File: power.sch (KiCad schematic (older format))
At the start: 75 parts, among them J6 7-17 V IN, Q1 DMP3099L-7, SW7 JS202011SCQN, U1 ICE40HX4K-TQ144, U10 MAX40200AUK, U12 TPS562201, U15 MAX40200AUK, U21 MAX40200AUK, U6 TLV62568APDRLR, U7 TLV62568APDRLR

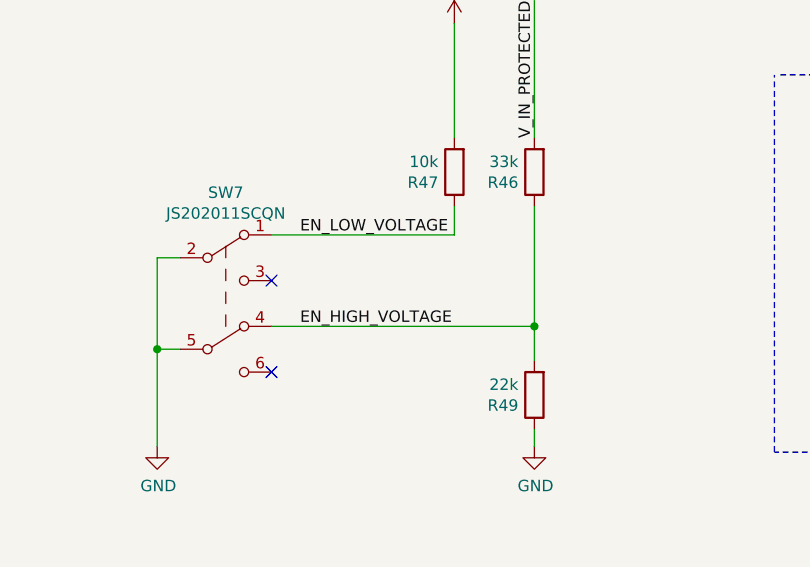
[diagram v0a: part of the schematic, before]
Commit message: Corrected a few footprints
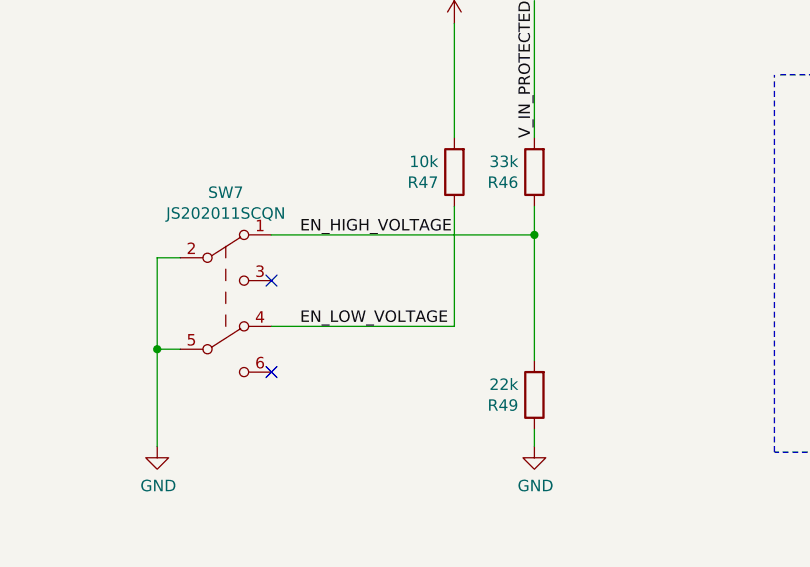
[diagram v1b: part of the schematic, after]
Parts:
- L3: footprint footprints:DLW5BTM_5.00x5.00mm_footprint -> footprints:L_Murata_DLW5BTM_5.00x5.00mm_footprint
- U6, U7: footprint Package_TO_SOT_SMD:SOT-563 -> footprints:Texas_DRL_SOT-563_1.6x1.6mm_0.5mm-pitch_footprint
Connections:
- net EN_HIGH_VOLTAGE: now also SW7.1 (A); no longer SW7.4 (A)
- net EN_LOW_VOLTAGE: now also SW7.4 (A); no longer SW7.1 (A)
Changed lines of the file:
@@
 F 0 "U6" H 2775 7815 50  0000 C CNN
 F 1 "TLV62568APDRLR" H 2775 7724 50  0000 C CNN
-F 2 "Package_TO_SOT_SMD:SOT-563" H 2775 7050 50  0001 C CNN
+F 2 "footprints:Texas_DRL_SOT-563_1.6x1.6mm_0.5mm-pitch_footprint" H 2775 7050 50  0001 C CNN
 F 3 "http://www.ti.com/lit/ds/symlink/tlv62568a.pdf" H 2775 7050 50  0001 C CNN
 F 4 "IC REG BUCK ADJUSTABLE 1A SOT563" H 0   0   50  0001 C CNN "Description"
@@
 F 0 "U7" H 2750 9765 50  0000 C CNN
 F 1 "TLV62568APDRLR" H 2750 9674 50  0000 C CNN
-F 2 "Package_TO_SOT_SMD:SOT-563" H 2750 9000 50  0001 C CNN
+F 2 "footprints:Texas_DRL_SOT-563_1.6x1.6mm_0.5mm-pitch_footprint" H 2750 9000 50  0001 C CNN
 F 3 "http://www.ti.com/lit/ds/symlink/tlv62568a.pdf" H 2750 9000 50  0001 C CNN
 F 4 "IC REG BUCK ADJUSTABLE 1A SOT563" H 0   0   50  0001 C CNN "Description"
@@
 $EndComp
 Wire Wire Line
-	10075 5300 11225 5300
-Wire Wire Line
-	10075 4900 10875 4900
+	10075 4900 11225 4900
+Wire Wire Line
+	10075 5300 10875 5300
 Wire Wire Line
 	9575 5825 9575 5400
@@
 Wire Wire Line
 	1700 9300 2300 9300
+Text Label 10200 4900 0    50   ~ 0
+EN_HIGH_VOLTAGE
 Text Label 10200 5300 0    50   ~ 0
-EN_HIGH_VOLTAGE
-Text Label 10200 4900 0    50   ~ 0
 EN_LOW_VOLTAGE
 $Comp
@@
 F 0 "L3" H 4000 1631 50  0000 C CNN
 F 1 "L_DLW5BTM" H 4000 1540 50  0000 C CNN
-F 2 "footprints:DLW5BTM_5.00x5.00mm_footprint" H 4000 1350 50  0001 C CNN
+F 2 "footprints:L_Murata_DLW5BTM_5.00x5.00mm_footprint" H 4000 1350 50  0001 C CNN
 F 3 "https://www.murata.com/en-us/products/productdata/8796761587742/EFLC0025.pdf" H 4000 1350 50  0001 C CNN
 F 4 "Murata Electronics North America" H 4000 1350 50  0001 C CNN "Mfg Name"
@@
 	13350 1725 14025 1725
 Connection ~ 14025 1725
-Wire Wire Line
-	11225 4775 11225 5300
-Wire Wire Line
-	10875 4900 10875 4775
-Connection ~ 11225 5300
-Wire Wire Line
-	11225 5300 11225 5450
 $Comp
 L Device:R R30
@@
 Text Notes 3550 6550 0    197  ~ 0
 1,2 V 1 A
+Wire Wire Line
+	11225 4775 11225 4900
+Wire Wire Line
+	10875 4775 10875 5300
+Connection ~ 11225 4900
+Wire Wire Line
+	11225 4900 11225 5450
 $EndSCHEMATC

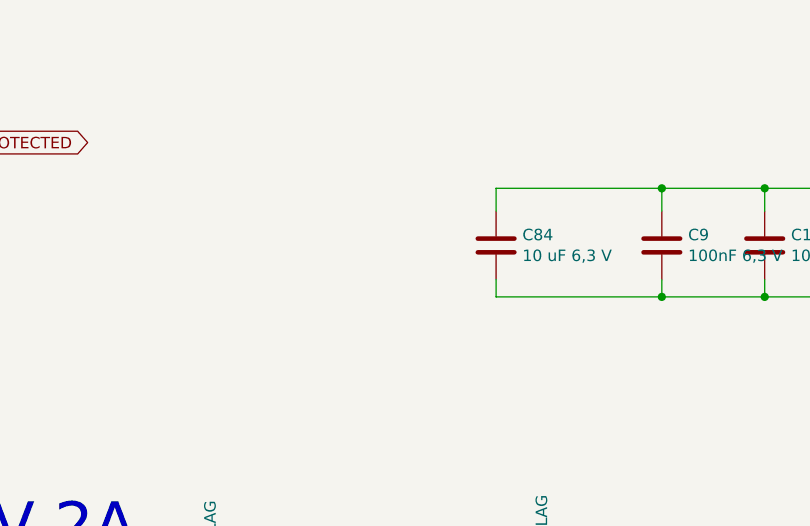
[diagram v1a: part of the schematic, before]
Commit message: Finished Silkscreen and added layer markings as specified by manufacturer
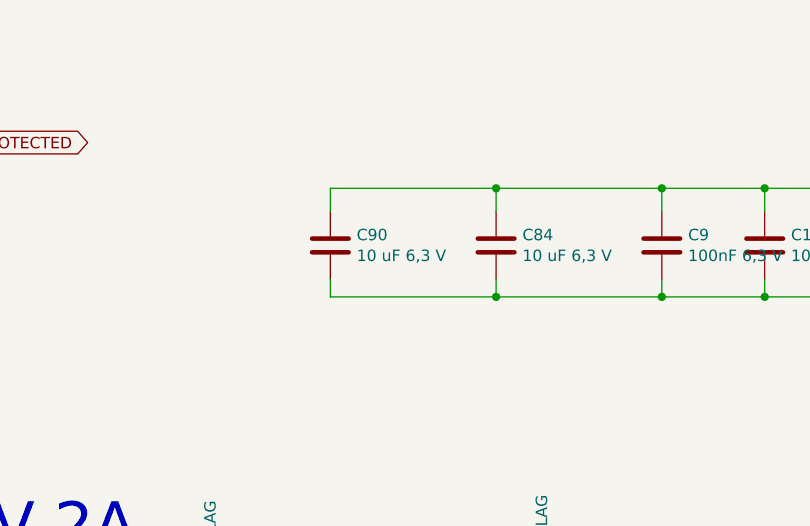
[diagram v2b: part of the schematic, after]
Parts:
- added C90: 10 uF 6,3 V, Capacitor_SMD:C_0603_1608Metric, symbol Device:C
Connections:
- net +3V3: now also C90.1
- net GND: now also C90.2
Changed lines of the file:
@@
 Wire Wire Line
 	11225 4900 11225 5450
+Wire Wire Line
+	7500 1750 8225 1750
+Wire Wire Line
+	7500 1675 7500 1750
+Wire Wire Line
+	7500 1275 8225 1275
+Wire Wire Line
+	7500 1375 7500 1275
+$Comp
+L Device:C C90
+U 1 1 5CE9322D
+P 7500 1525
+AR Path="/5CA8FBC7/5CE9322D" Ref="C90"  Part="1"
+AR Path="/5CAB8B22/5CE9322D" Ref="C?"  Part="1"
+F 0 "C90" H 7615 1571 50  0000 L CNN
+F 1 "10 uF 6,3 V" H 7615 1480 50  0000 L CNN
+F 2 "Capacitor_SMD:C_0603_1608Metric" H 7538 1375 50  0001 C CNN
+F 3 "~" H 7500 1525 50  0001 C CNN
+F 4 "Samsung Electro-Mechanics" H 7500 1525 50  0001 C CNN "Mfg Name"
+F 5 "CL10A106MQ8NNNC" H 7500 1525 50  0001 C CNN "Mfg Part Num"
+F 6 "1276-1119-1-ND" H 7500 1525 50  0001 C CNN "Digikey"
+F 7 " CAP CER 10UF 6.3V X5R 0603" H 7500 1525 50  0001 C CNN "Description"
+F 8 "Any" H -725 0   50  0001 C CNN "Spec"
+	1    7500 1525
+	1    0    0    -1
+$EndComp
+Connection ~ 8225 1275
+Connection ~ 8225 1750
 $EndSCHEMATC

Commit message: More complete BOM
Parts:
- C1, C3, C4, C5, C50, C52, C7, C8, C83, C84, C89, C90: Description CAP CER 10UF 6.3V X5R 0603 -> CAP CER 10UF 6.3V X5R 0603
- D9: Description (none) -> LED RED DIFFUSED 1608 SMD; Digikey (none) -> SML-D12U1WT86CT-ND; Mfg Name (none) -> Rohm Semiconductor; Mfg Part Num (none) -> SML-D12U1WT86; Spec (none) -> Any
- R14, R15: Description (none) -> RES SMD 100K OHM 1% 1/10W 0603; Digikey (none) -> 311-100KHRCT-ND; Mfg Name (none) -> Yageo; Mfg Part Num (none) -> RC0603FR-07100KL; Spec (none) -> Any
- R16: Description (none) -> RES SMD 220K OHM 1% 1/10W 0603; Digikey (none) -> 311-220KHRCT-ND; Mfg Name (none) -> Yageo; Mfg Part Num (none) -> RC0603FR-07220KL; Spec (none) -> Any
- R17: Description (none) -> RES SMD 48.7K OHM 1% 1/10W 0603; Digikey (none) -> 311-48.7KHRCT-ND; Mfg Name (none) -> Yageo; Mfg Part Num (none) -> RC0603FR-0748K7L; Spec (none) -> Any
- R18, R47, R48, R67: Description (none) -> RES 10K OHM 5% 1/10W 0603; Digikey (none) -> RMCF0603JT10K0CT-ND; Mfg Name (none) -> Stackpole Electronics Inc; Mfg Part Num (none) -> RMCF0603JT10K0; Spec (none) -> Any
- R19: Description (none) -> RES 560 OHM 5% 1/8W 0603; Digikey (none) -> 2019-RK73B1JTTD561JCT-ND; Mfg Name (none) -> KOA Speer Electronics, Inc.; Mfg Part Num (none) -> RK73B1JTTD561J; Spec (none) -> Any
- R30: Description (none) -> RES SMD 0 OHM JUMPER 1/8W 0805; Digikey (none) -> 311-0.0ARCT-ND; Mfg Name (none) -> Yageo; Mfg Part Num (none) -> RC0805JR-070RL; Spec (none) -> Any
- R35: Description (none) -> RES SMD 54.9K OHM 1% 1/10W 0603; Digikey (none) -> 311-54.9KHRCT-ND; Mfg Name (none) -> Yageo; Mfg Part Num (none) -> RC0603FR-0754K9L; Spec (none) -> Any
- R40: Description (none) -> RES SMD 10K OHM 1% 1/10W 0603; Digikey (none) -> 311-10.0KHRCT-ND; Mfg Name (none) -> Yageo; Mfg Part Num (none) -> RC0603FR-0710KL; Spec (none) -> Any
- R41, R42: Description (none) -> RES 100 OHM 1% 1/10W 0603; Digikey (none) -> RMCF0603FT100RCT-ND; Mfg Name (none) -> Stackpole Electronics Inc; Mfg Part Num (none) -> RMCF0603FT100R; Spec (none) -> Any
- R46: Description (none) -> RES SMD 33K OHM 5% 1/10W 0603; Digikey (none) -> 311-33KGRCT-ND; Mfg Name (none) -> Yageo; Mfg Part Num (none) -> RC0603JR-0733KL; Spec (none) -> Any
- R49: Description (none) -> RES SMD 22K OHM 1% 1/10W 0603; Digikey (none) -> 311-22.0KHRCT-ND; Mfg Name (none) -> Yageo; Mfg Part Num (none) -> RC0603FR-0722KL; Spec (none) -> Any
